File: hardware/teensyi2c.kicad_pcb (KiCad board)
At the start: 2 copper layers, 51 x 51.7 mm, 14 parts, among them J1 TEENSY3.2-72MHz, J2 OLED-I2C, J3 ADAFRUIT_BME280, U1 ESP-01v090

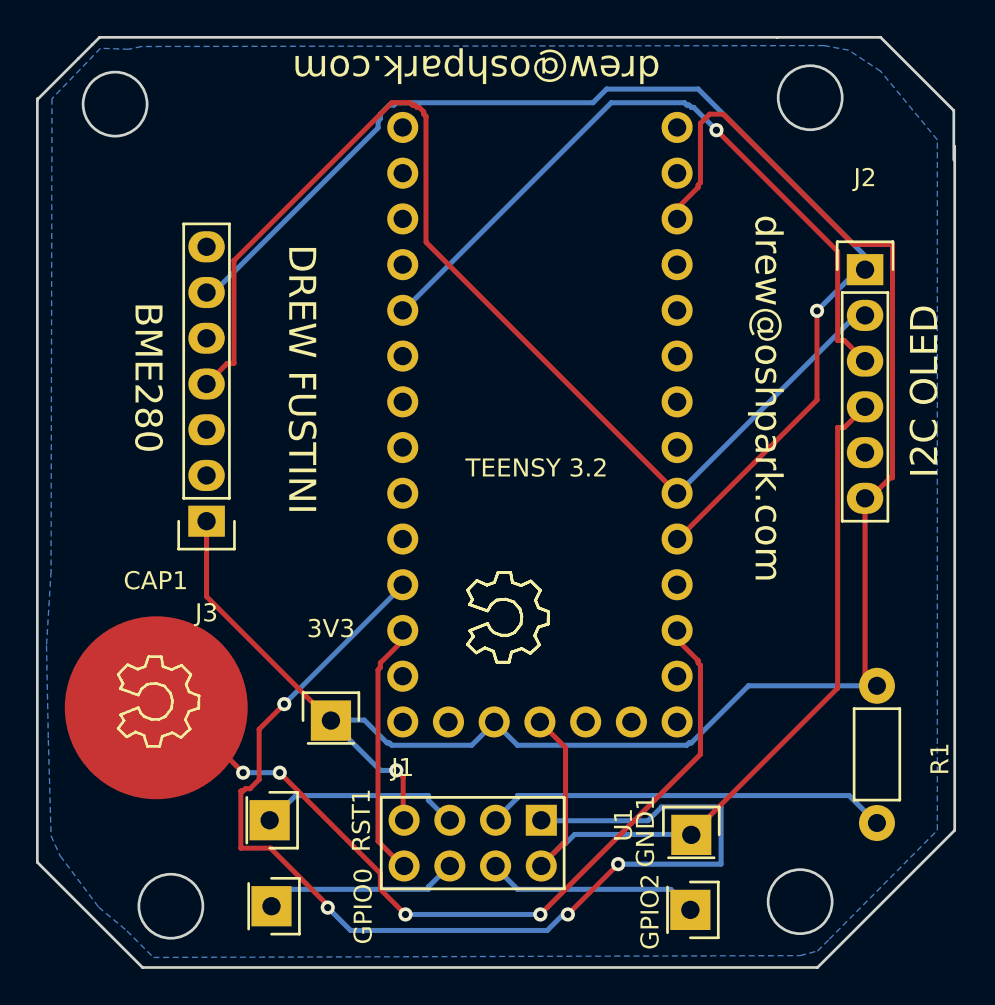
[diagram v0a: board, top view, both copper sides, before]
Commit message: fix gnd air wire
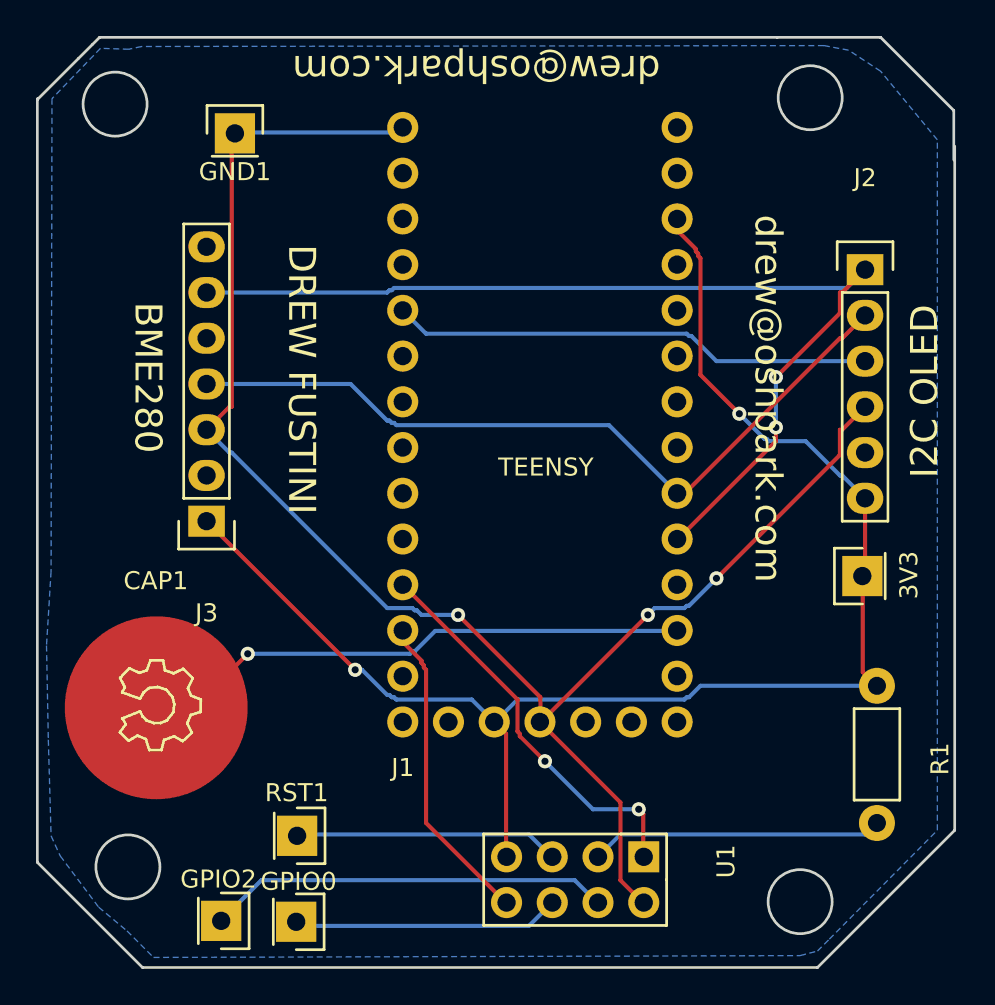
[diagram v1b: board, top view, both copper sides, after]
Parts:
- removed the REF** at (148.6, 88.1) (x2)
- moved GND1 46.5 mm to (133.7, 61.3)
- moved 3V3 30.6 mm to (168.5, 85.9), turned to 90 degrees
- moved GPIO2 26.1 mm to (132.9, 105.0)
- moved U1 6.04 mm to (156.4, 101.4)
- moved RST1 1.75 mm to (137.1, 100.3)
- moved GPIO0 1.62 mm to (137.1, 105.1)
- moved REF** 0.23 mm to (129.3, 93.0)
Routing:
- net /GND: track 46.5 -> 91.5 mm, vias 0 -> 3
- net Net-(J1-Pad9): track 62.3 -> 22.2 mm, vias 4 -> 2
- net /SCK: track 63.6 -> 43.2 mm
- net /VIN: track 100.8 -> 82.5 mm, vias 1 -> 2
- net Net-(CAP1-Pad1): track 46.6 -> 30.8 mm, vias 4 -> 1
- net /RST: track 39.3 -> 26.8 mm, vias 1 -> 0
- net Net-(GPIO2-Pad1): track 12.0 -> 22.5 mm
- net /SDA: track 65.8 -> 56.5 mm, vias 1 -> 2
- net Net-(R1-Pad2): track 22.6 -> 16.3 mm
- net Net-(GPIO0-Pad1): track 10.9 -> 14.9 mm
- net Net-(RST1-Pad1): track 11.3 -> 14.7 mm
- net Net-(J1-Pad10): track 14.3 -> 17.5 mm
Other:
- outline, holes or cut-outs redrawn
- net class Default: clearance 0.2794 -> 0.2286; trace_width 0.2794 -> 0.2286
- rule trace_clearance: 0.2794 -> 0.2286
- rule trace_min: 0.254 -> 0.2286

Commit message: fix i2c bus pins
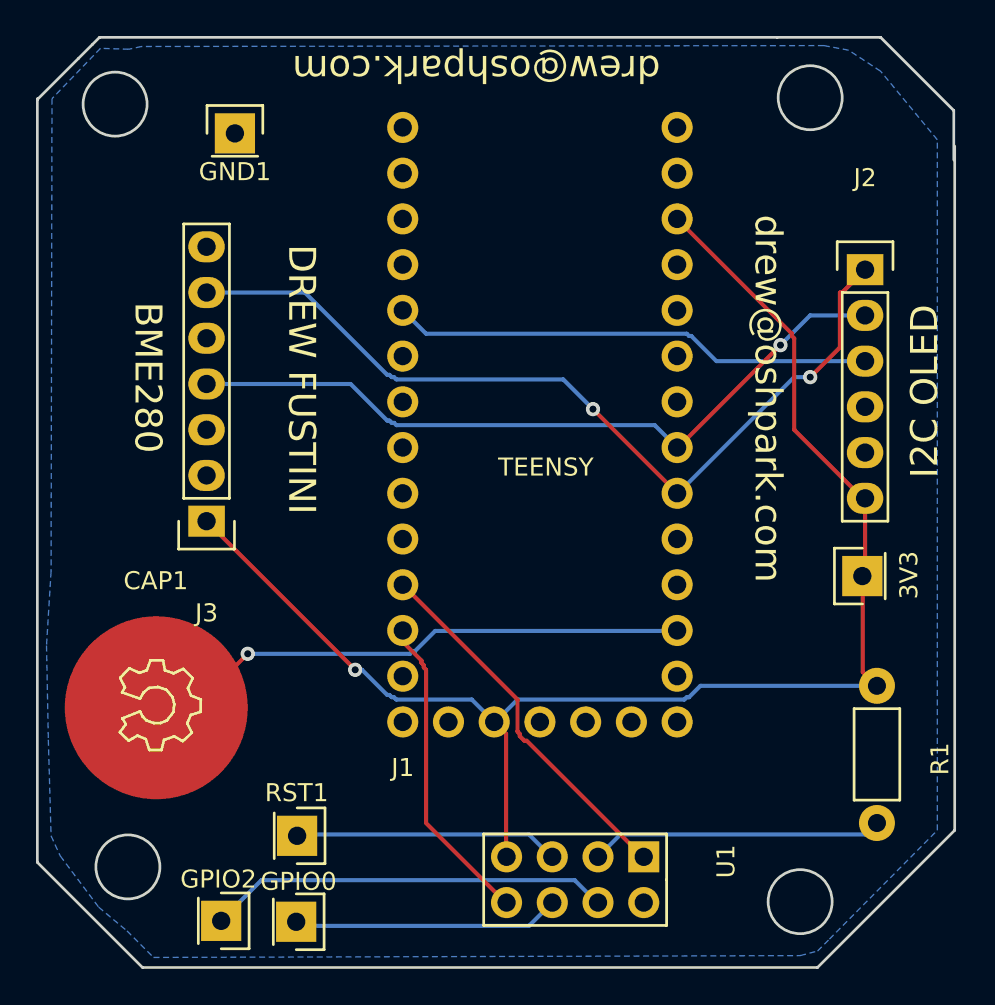
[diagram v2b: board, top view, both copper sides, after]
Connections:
- J1 pad 17: /SDA -> Net-(J1-Pad17)
- J1 pad 18: /SCK -> /SDA
- J1 pad 19: Net-(J1-Pad19) -> /SCK
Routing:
- net /GND: track 91.5 -> 0.00 mm, vias 3 -> 0
- net /SDA: track 56.5 -> 48.1 mm
- net /SCK: track 43.2 -> 41.1 mm, vias 0 -> 1
- net Net-(J1-Pad9): track 22.2 -> 20.8 mm, vias 2 -> 0
- net /VIN: track 82.5 -> 81.3 mm, vias 2 -> 1
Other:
- board text added: "2016-08-05"

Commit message: add commit and github url to silkscreen
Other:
- board text added: "commit: bf1d95b"
- board text added: "https://github.com/pdp7/teensy-weather-badge"
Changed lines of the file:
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@@
     (links 23)
     (no_connects 0)
-    (area 121.539 55.753 173.863 124.587)
+    (area 121.57158 55.855799 173.82012 124.612401)
     (thickness 1.6)
-    (drawings 26)
+    (drawings 28)
     (tracks 114)
     (zones 0)
@@
       (net 36 "Net-(CAP1-Pad1)") (clearance 0.508))
   )
+  (gr_text "commit: bf1d95b" (at 164.1856 90.297 270) (layer B.SilkS)
+    (effects (font (size 1.27 1.27) (thickness 0.1778)) (justify mirror))
+  )
+  (gr_text https://github.com/pdp7/teensy-weather-badge (at 161.4424 79.0448 270) (layer B.SilkS)
+    (effects (font (size 1.016 1.016) (thickness 0.1524)) (justify mirror))
+  )
   (gr_text 2016-08-05 (at 152.2476 106.2736 180) (layer B.SilkS)
